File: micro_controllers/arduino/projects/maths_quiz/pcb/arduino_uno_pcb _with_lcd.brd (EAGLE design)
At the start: 70.8 x 55.9 mm, 13 parts, among them IC1 ATMEGA328, Q1 16MHZ

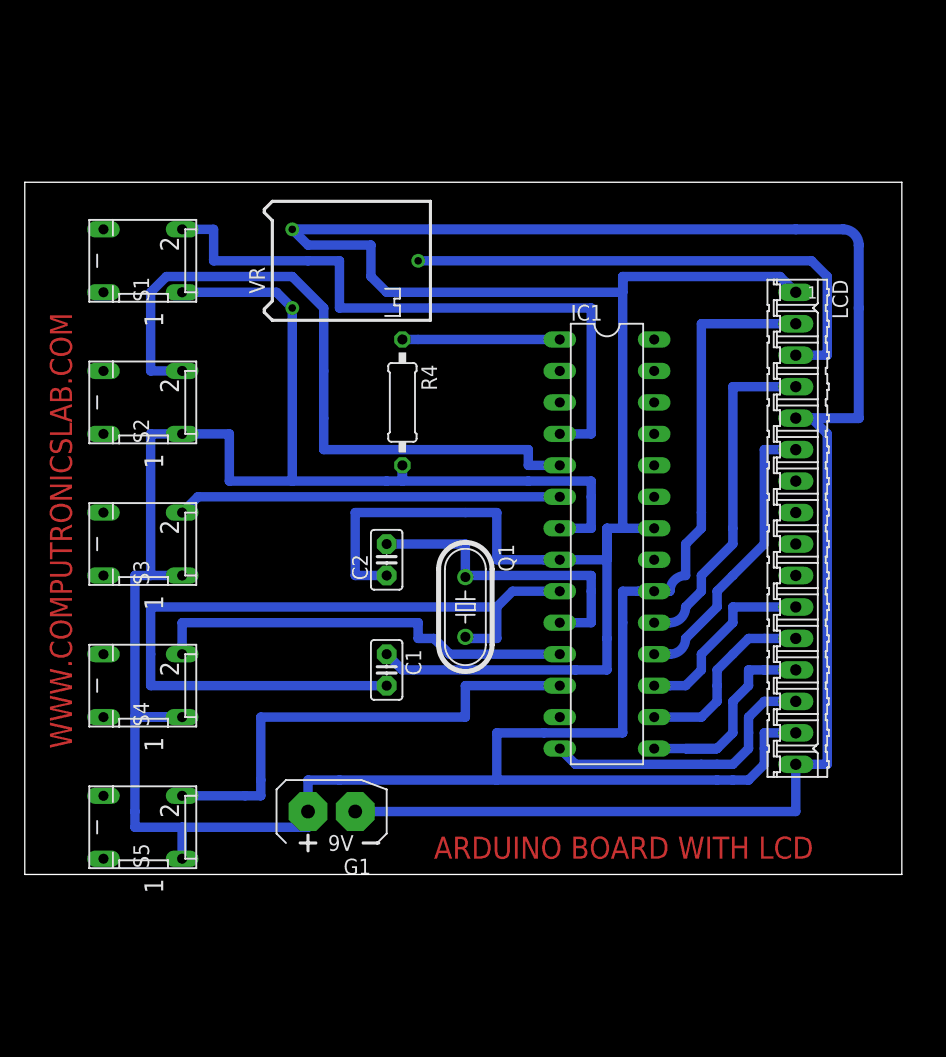
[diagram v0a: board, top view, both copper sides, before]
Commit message: 
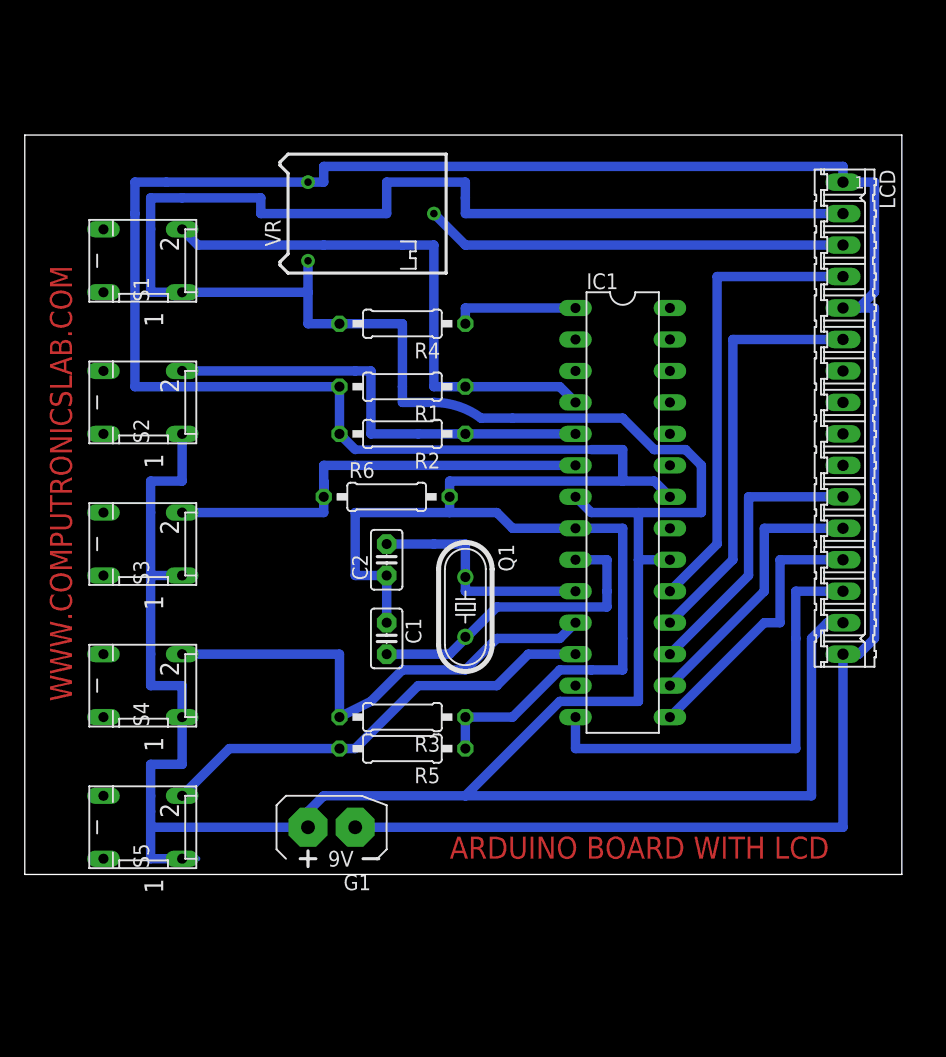
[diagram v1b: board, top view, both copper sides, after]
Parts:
- added R1, R2, R3, R5, R6: 10K, rcl:0207/10
- moved LCD 9.67 mm to (101.6, 45.7)
- moved R4 6.35 mm to (66.0, 53.3), turned to 180 degrees
- moved VR 4.02 mm to (61.0, 62.2)
- moved IC1 2.84 mm to (83.8, 38.1)
- moved C1 2.54 mm to (64.8, 27.9)
- moved G1 1.27 mm to (61.0, 12.7)
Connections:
- removed net N$28: C1.1, C2.1, G1.-, IC1.22, IC1.8, LCD.1, LCD.16, LCD.5, VR.3
- new net N$6: C1.1, C2.1, G1.-, IC1.22, IC1.8, LCD.1, LCD.16, LCD.5, R1.2, R2.2, R3.1, R5.1, R6.2, VR.3
- net N$4: now also R3.2
- net N$5: now also R1.1
- net N$7: now also R2.1
- net N$8: now also R6.1
- net N$9: now also R5.2
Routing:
- net N$6: track 0.00 -> 305.2 mm
- net N$28: track 271.1 -> 0.00 mm
- net N$3: track 237.1 -> 303.7 mm
- net N$1: track 64.2 -> 26.0 mm
- net N$7: track 56.2 -> 36.8 mm
- net N$29: track 23.2 -> 36.8 mm
- net N$24: track 23.5 -> 33.9 mm
- net N$23: track 27.5 -> 37.1 mm
- net N$22: track 42.4 -> 34.1 mm
- net N$5: track 52.1 -> 44.2 mm
- net N$25: track 15.5 -> 23.0 mm
- net N$8: track 31.0 -> 38.1 mm
- net N$26: track 15.5 -> 22.2 mm
- net N$2: track 25.7 -> 19.3 mm
- net N$4: track 34.8 -> 39.8 mm
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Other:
- board size 70.8 x 55.9 mm -> 70.8 x 59.7 mm

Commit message: 
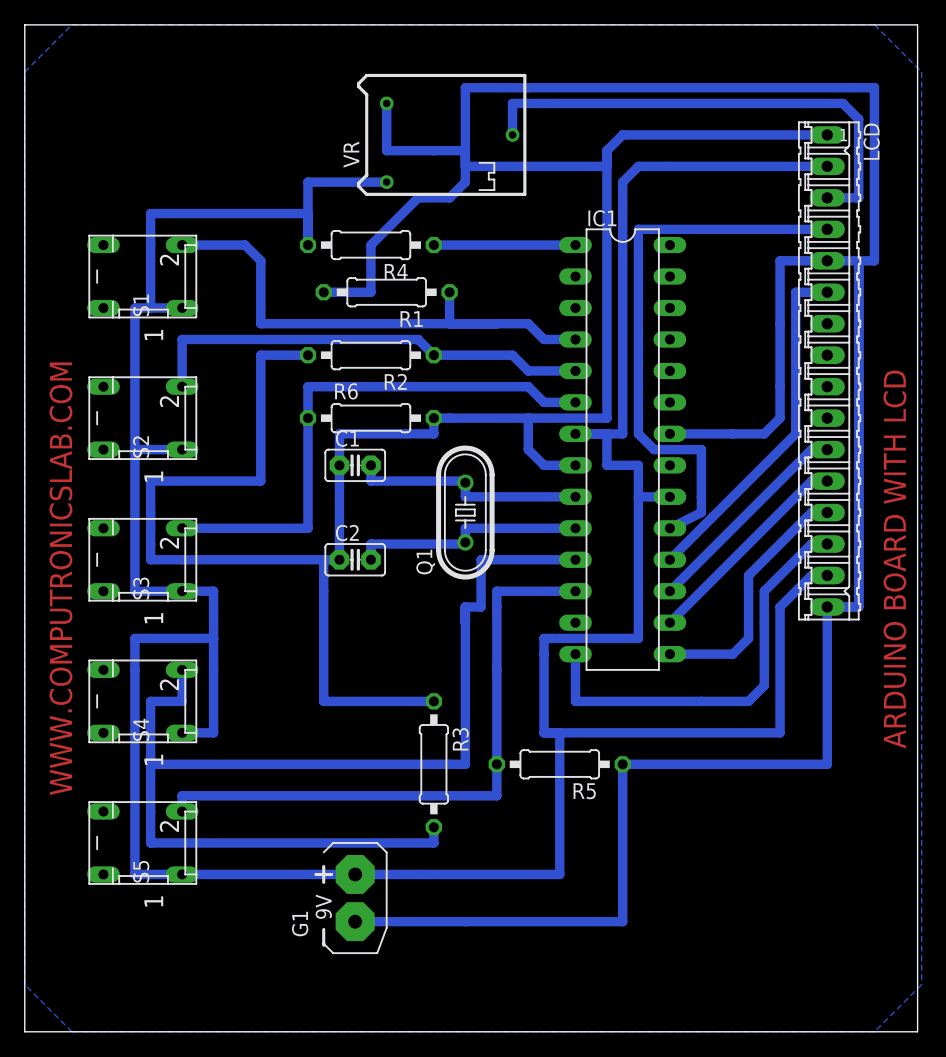
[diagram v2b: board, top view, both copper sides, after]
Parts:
- moved C1 14.2 mm to (62.2, 41.9), turned to 0 degrees
- moved R5 12.8 mm to (78.7, 17.8)
- moved VR 8.98 mm to (67.3, 68.6)
- moved R1 7.73 mm to (64.8, 55.9)
- moved Q1 7.62 mm to (71.1, 38.1), turned to 90 degrees
- moved R2 6.84 mm to (63.5, 50.8)
- moved R4 6.84 mm to (63.5, 59.7)
- moved R6 6.48 mm to (63.5, 45.7)
- moved G1 6.48 mm to (62.2, 6.35), turned to 0 degrees
- moved IC1 5.08 mm to (83.8, 43.2)
- moved R3 4.58 mm to (68.6, 17.8), turned to 270 degrees
- moved LCD 4.02 mm to (100.3, 49.5)
- moved C2 2.54 mm to (62.2, 34.3), turned to 0 degrees
- moved S1 1.27 mm to (45.7, 57.1)
- moved S2 1.27 mm to (45.7, 45.7)
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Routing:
- net N$6: track 305.2 -> 394.8 mm
- net N$4: track 39.8 -> 94.0 mm
- net N$3: track 303.7 -> 272.1 mm
- net N$9: track 36.5 -> 49.5 mm
- net N$23: track 37.1 -> 45.3 mm
- net N$1: track 26.0 -> 19.3 mm
- net N$22: track 34.1 -> 39.9 mm
- net N$8: track 38.1 -> 43.7 mm
- net N$24: track 33.9 -> 28.3 mm
- net N$25: track 23.0 -> 17.4 mm
- net N$26: track 22.2 -> 17.4 mm
- net N$29: track 36.8 -> 33.9 mm
- net N$27: track 22.2 -> 20.4 mm
- net N$31: track 10.2 -> 11.4 mm
- added copper zone on layer 16, net N$10
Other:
- board size 70.8 x 59.7 mm -> 72.1 x 81.3 mm
